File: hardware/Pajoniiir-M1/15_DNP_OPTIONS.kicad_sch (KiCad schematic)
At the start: 0 parts

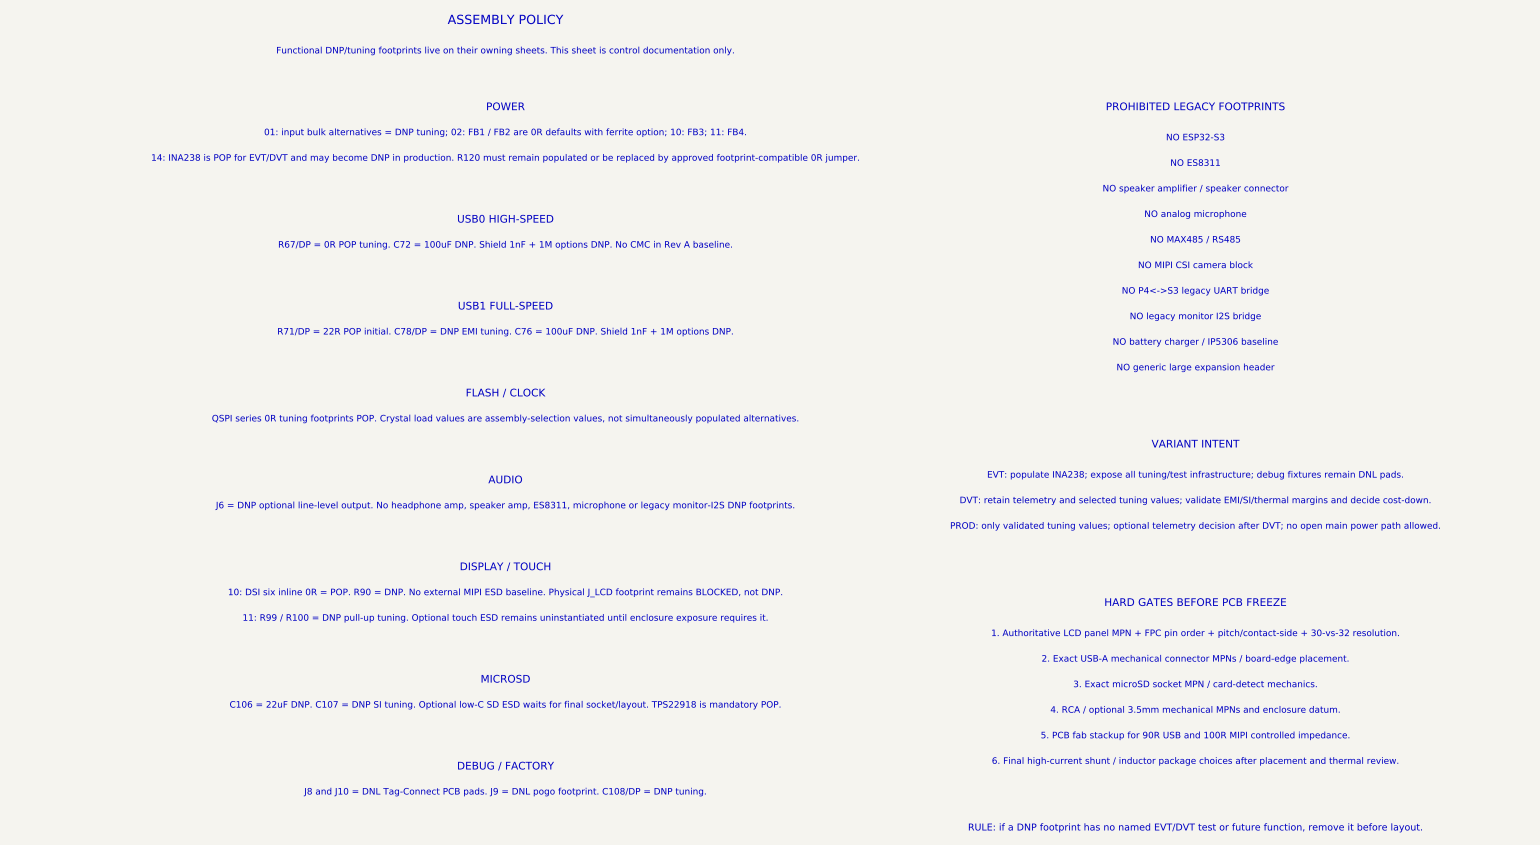
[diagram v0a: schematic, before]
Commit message: hardware: constrain RefDes migration to annotation fields
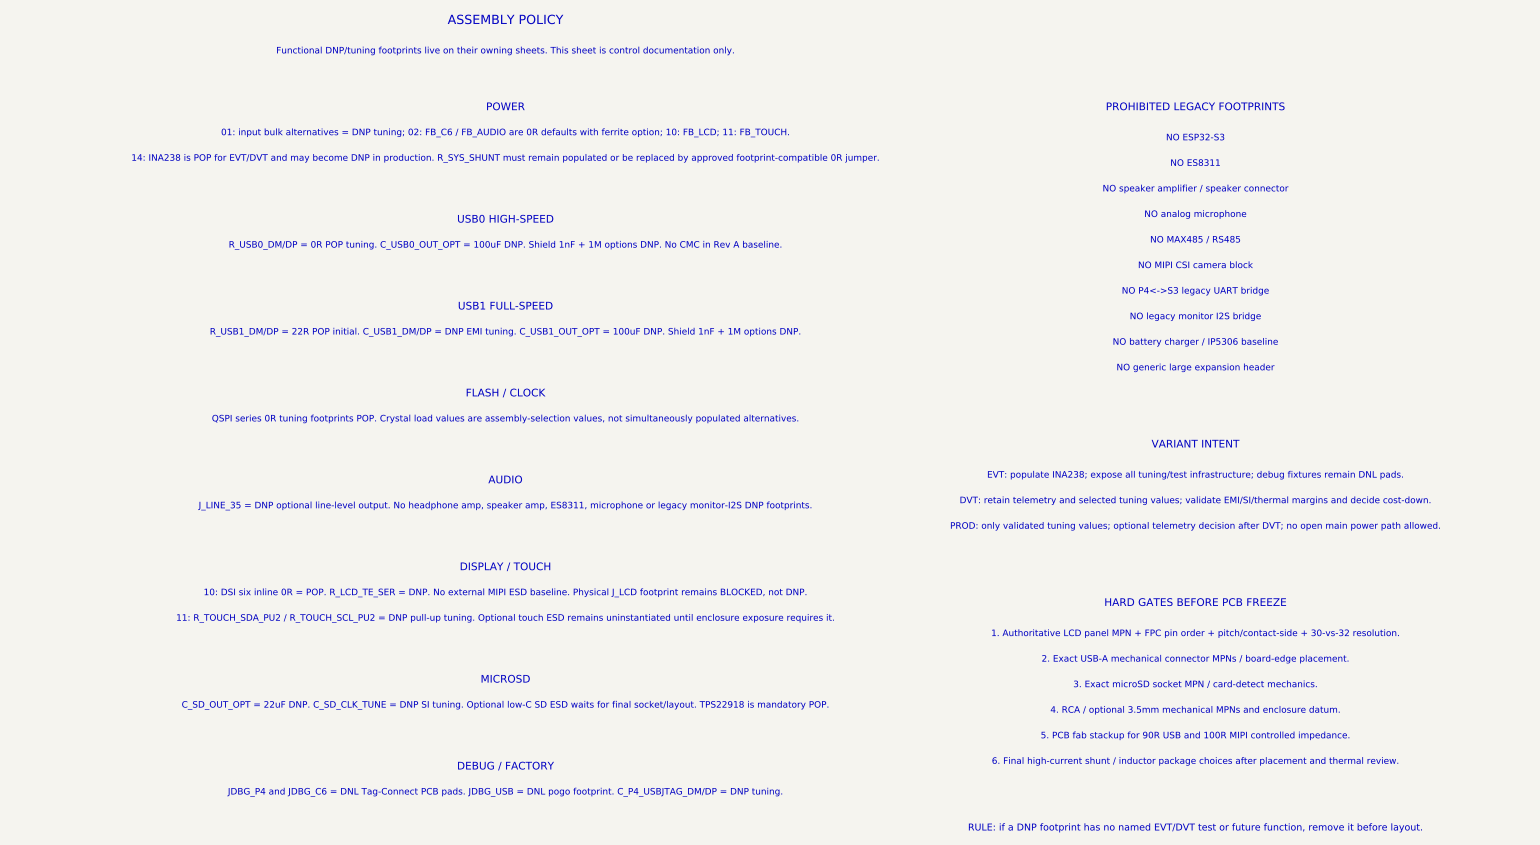
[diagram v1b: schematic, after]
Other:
- note added: "01: input bulk alternatives = DNP tuning; 02: FB_C6 / FB_AUDIO are 0R defaults with ferrite option; 10: FB_LCD; 11: FB_TOUCH."
- note added: "10: DSI six inline 0R = POP. R_LCD_TE_SER = DNP. No external MIPI ESD baseline. Physical J_LCD footprint remains BLOCKED, not DNP."
- note added: "11: R_TOUCH_SDA_PU2 / R_TOUCH_SCL_PU2 = DNP pull-up tuning. Optional touch ESD remains uninstantiated until enclosure exposure requires it."
- note added: "14: INA238 is POP for EVT/DVT and may become DNP in production. R_SYS_SHUNT must remain populated or be replaced by approved footprint-compatible 0R jumper."
- note added: "C_SD_OUT_OPT = 22uF DNP. C_SD_CLK_TUNE = DNP SI tuning. Optional low-C SD ESD waits for final socket/layout. TPS22918 is mandatory POP."
- note added: "JDBG_P4 and JDBG_C6 = DNL Tag-Connect PCB pads. JDBG_USB = DNL pogo footprint. C_P4_USBJTAG_DM/DP = DNP tuning."
- note added: "J_LINE_35 = DNP optional line-level output. No headphone amp, speaker amp, ES8311, microphone or legacy monitor-I2S DNP footprints."
- note added: "R_USB0_DM/DP = 0R POP tuning. C_USB0_OUT_OPT = 100uF DNP. Shield 1nF + 1M options DNP. No CMC in Rev A baseline."
- note added: "R_USB1_DM/DP = 22R POP initial. C_USB1_DM/DP = DNP EMI tuning. C_USB1_OUT_OPT = 100uF DNP. Shield 1nF + 1M options DNP."
- note removed: "01: input bulk alternatives = DNP tuning; 02: FB1 / FB2 are 0R defaults with ferrite option; 10: FB3; 11: FB4."
- note removed: "10: DSI six inline 0R = POP. R90 = DNP. No external MIPI ESD baseline. Physical J_LCD footprint remains BLOCKED, not DNP."
- note removed: "11: R99 / R100 = DNP pull-up tuning. Optional touch ESD remains uninstantiated until enclosure exposure requires it."
- note removed: "14: INA238 is POP for EVT/DVT and may become DNP in production. R120 must remain populated or be replaced by approved footprint-compatible 0R jumper."
- note removed: "C106 = 22uF DNP. C107 = DNP SI tuning. Optional low-C SD ESD waits for final socket/layout. TPS22918 is mandatory POP."
- note removed: "J6 = DNP optional line-level output. No headphone amp, speaker amp, ES8311, microphone or legacy monitor-I2S DNP footprints."
- note removed: "J8 and J10 = DNL Tag-Connect PCB pads. J9 = DNL pogo footprint. C108/DP = DNP tuning."
- note removed: "R67/DP = 0R POP tuning. C72 = 100uF DNP. Shield 1nF + 1M options DNP. No CMC in Rev A baseline."
- note removed: "R71/DP = 22R POP initial. C78/DP = DNP EMI tuning. C76 = 100uF DNP. Shield 1nF + 1M options DNP."
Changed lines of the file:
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@@
   (text "Functional DNP/tuning footprints live on their owning sheets. This sheet is control documentation only." (exclude_from_sim no) (at 35 31 0) (effects (font (size 1.27 1.27))))
   (text "POWER" (exclude_from_sim no) (at 35 42 0) (effects (font (size 1.5 1.5))))
-  (text "01: input bulk alternatives = DNP tuning; 02: FB1 / FB2 are 0R defaults with ferrite option; 10: FB3; 11: FB4." (exclude_from_sim no) (at 35 47 0) (effects (font (size 1.27 1.27))))
-  (text "14: INA238 is POP for EVT/DVT and may become DNP in production. R120 must remain populated or be replaced by approved footprint-compatible 0R jumper." (exclude_from_sim no) (at 35 52 0) (effects (font (size 1.27 1.27))))
+  (text "01: input bulk alternatives = DNP tuning; 02: FB_C6 / FB_AUDIO are 0R defaults with ferrite option; 10: FB_LCD; 11: FB_TOUCH." (exclude_from_sim no) (at 35 47 0) (effects (font (size 1.27 1.27))))
+  (text "14: INA238 is POP for EVT/DVT and may become DNP in production. R_SYS_SHUNT must remain populated or be replaced by approved footprint-compatible 0R jumper." (exclude_from_sim no) (at 35 52 0) (effects (font (size 1.27 1.27))))
   (text "USB0 HIGH-SPEED" (exclude_from_sim no) (at 35 64 0) (effects (font (size 1.5 1.5))))
-  (text "R67/DP = 0R POP tuning. C72 = 100uF DNP. Shield 1nF + 1M options DNP. No CMC in Rev A baseline." (exclude_from_sim no) (at 35 69 0) (effects (font (size 1.27 1.27))))
+  (text "R_USB0_DM/DP = 0R POP tuning. C_USB0_OUT_OPT = 100uF DNP. Shield 1nF + 1M options DNP. No CMC in Rev A baseline." (exclude_from_sim no) (at 35 69 0) (effects (font (size 1.27 1.27))))
   (text "USB1 FULL-SPEED" (exclude_from_sim no) (at 35 81 0) (effects (font (size 1.5 1.5))))
-  (text "R71/DP = 22R POP initial. C78/DP = DNP EMI tuning. C76 = 100uF DNP. Shield 1nF + 1M options DNP." (exclude_from_sim no) (at 35 86 0) (effects (font (size 1.27 1.27))))
+  (text "R_USB1_DM/DP = 22R POP initial. C_USB1_DM/DP = DNP EMI tuning. C_USB1_OUT_OPT = 100uF DNP. Shield 1nF + 1M options DNP." (exclude_from_sim no) (at 35 86 0) (effects (font (size 1.27 1.27))))
   (text "FLASH / CLOCK" (exclude_from_sim no) (at 35 98 0) (effects (font (size 1.5 1.5))))
   (text "QSPI series 0R tuning footprints POP. Crystal load values are assembly-selection values, not simultaneously populated alternatives." (exclude_from_sim no) (at 35 103 0) (effects (font (size 1.27 1.27))))
   (text "AUDIO" (exclude_from_sim no) (at 35 115 0) (effects (font (size 1.5 1.5))))
-  (text "J6 = DNP optional line-level output. No headphone amp, speaker amp, ES8311, microphone or legacy monitor-I2S DNP footprints." (exclude_from_sim no) (at 35 120 0) (effects (font (size 1.27 1.27))))
+  (text "J_LINE_35 = DNP optional line-level output. No headphone amp, speaker amp, ES8311, microphone or legacy monitor-I2S DNP footprints." (exclude_from_sim no) (at 35 120 0) (effects (font (size 1.27 1.27))))
   (text "DISPLAY / TOUCH" (exclude_from_sim no) (at 35 132 0) (effects (font (size 1.5 1.5))))
-  (text "10: DSI six inline 0R = POP. R90 = DNP. No external MIPI ESD baseline. Physical J_LCD footprint remains BLOCKED, not DNP." (exclude_from_sim no) (at 35 137 0) (effects (font (size 1.27 1.27))))
-  (text "11: R99 / R100 = DNP pull-up tuning. Optional touch ESD remains uninstantiated until enclosure exposure requires it." (exclude_from_sim no) (at 35 142 0) (effects (font (size 1.27 1.27))))
+  (text "10: DSI six inline 0R = POP. R_LCD_TE_SER = DNP. No external MIPI ESD baseline. Physical J_LCD footprint remains BLOCKED, not DNP." (exclude_from_sim no) (at 35 137 0) (effects (font (size 1.27 1.27))))
+  (text "11: R_TOUCH_SDA_PU2 / R_TOUCH_SCL_PU2 = DNP pull-up tuning. Optional touch ESD remains uninstantiated until enclosure exposure requires it." (exclude_from_sim no) (at 35 142 0) (effects (font (size 1.27 1.27))))
   (text "MICROSD" (exclude_from_sim no) (at 35 154 0) (effects (font (size 1.5 1.5))))
-  (text "C106 = 22uF DNP. C107 = DNP SI tuning. Optional low-C SD ESD waits for final socket/layout. TPS22918 is mandatory POP." (exclude_from_sim no) (at 35 159 0) (effects (font (size 1.27 1.27))))
+  (text "C_SD_OUT_OPT = 22uF DNP. C_SD_CLK_TUNE = DNP SI tuning. Optional low-C SD ESD waits for final socket/layout. TPS22918 is mandatory POP." (exclude_from_sim no) (at 35 159 0) (effects (font (size 1.27 1.27))))
   (text "DEBUG / FACTORY" (exclude_from_sim no) (at 35 171 0) (effects (font (size 1.5 1.5))))
-  (text "J8 and J10 = DNL Tag-Connect PCB pads. J9 = DNL pogo footprint. C108/DP = DNP tuning." (exclude_from_sim no) (at 35 176 0) (effects (font (size 1.27 1.27))))
+  (text "JDBG_P4 and JDBG_C6 = DNL Tag-Connect PCB pads. JDBG_USB = DNL pogo footprint. C_P4_USBJTAG_DM/DP = DNP tuning." (exclude_from_sim no) (at 35 176 0) (effects (font (size 1.27 1.27))))
   (text "PROHIBITED LEGACY FOOTPRINTS" (exclude_from_sim no) (at 170 42 0) (effects (font (size 1.5 1.5))))
   (text "NO ESP32-S3" (exclude_from_sim no) (at 170 48 0) (effects (font (size 1.27 1.27))))
